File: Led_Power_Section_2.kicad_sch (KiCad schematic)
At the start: 11 parts, among them IC2 A6214KLKTR-T

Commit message: fixing review suggestions
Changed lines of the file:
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@@
 		)
 	)
-	(global_label "LED_6"
-		(shape input)
+	(hierarchical_label "LED_6"
+		(shape output)
 		(at 118.11 40.64 0)
 		(fields_autoplaced yes)
@@
 			(justify left)
 		)
-		(property "Intersheetrefs" "${INTERSHEET_REFS}"
-			(at 126.7194 40.64 0)
-			(effects
-				(font
-					(size 1.27 1.27)
-				)
-				(justify left)
-				(hide yes)
+	)
+	(hierarchical_label "I_LED_6"
+		(shape output)
+		(at 118.11 33.02 0)
+		(fields_autoplaced yes)
+		(effects
+			(font
+				(size 1.27 1.27)
 			)
+			(justify left)
 		)
 	)
-	(global_label "ADIM_0"
+	(hierarchical_label "ADIM_0"
 		(shape input)
 		(at 53.34 39.37 180)
@@
 			(justify right)
 		)
-		(property "Intersheetrefs" "${INTERSHEET_REFS}"
-			(at 43.7629 39.37 0)
-			(effects
-				(font
-					(size 1.27 1.27)
-				)
-				(justify right)
-				(hide yes)
-			)
-		)
 	)
-	(global_label "I_LED_6"
-		(shape input)
-		(at 118.11 33.02 0)
-		(fields_autoplaced yes)
-		(effects
-			(font
-				(size 1.27 1.27)
-			)
-			(justify left)
-		)
-		(property "Intersheetrefs" "${INTERSHEET_REFS}"
-			(at 128.2918 33.02 0)
-			(effects
-				(font
-					(size 1.27 1.27)
-				)
-				(justify left)
-				(hide yes)
-			)
-		)
-	)

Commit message: first complete version schematics
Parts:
- added C40, C44, C48, C52, C56: 33 uF, Capacitor_THT:CP_Radial_D8.0mm_P3.50mm, symbol PCM_SL_Devices:Capacitor_PO
- added C41, C45, C49, C53, C57: 4.7 uF, Capacitor_THT:C_Disc_D3.0mm_W2.0mm_P2.50mm, symbol PCM_SL_Devices:Capacitor_NP
- added C42, C46, C50, C54, C58: 1 uF, Capacitor_SMD:C_1206_3216Metric_Pad1.33x1.80mm_HandSolder, symbol PCM_SL_Devices:Capacitor_NP
- added C43, C47, C51, C55, C59: 0.1 uF, Capacitor_SMD:C_1206_3216Metric_Pad1.33x1.80mm_HandSolder, symbol PCM_SL_Devices:Capacitor_NP
- added D10, D11, D12, D8, D9: 30V 2A, ADC:SODFL3516X90N, symbol PCM_4ms_Diode:B140-E3
- added IC10, IC11, IC12, IC13, IC9: A6214KLKTR-T, LED_Driver:SOP100P600X165-11N, symbol A6214KLKTR-T:A6214KLKTR-T
- added L10, L11, L12, L8, L9: 47 uH 2A, ADC:CDRH105RNP151NC, symbol Device:L
- added R21, R22, R25, R26, R29, R30, R33, R34, R37, R38: 10k, Resistor_SMD:R_1206_3216Metric_Pad1.30x1.75mm_HandSolder, symbol PCM_SL_Resistors:Resistor
- added R23, R27, R31, R35, R39: 442k, Resistor_SMD:R_1206_3216Metric_Pad1.30x1.75mm_HandSolder, symbol PCM_SL_Resistors:Resistor
- added R24, R28, R32, R36, R40: R120 or R260, Resistor_THT:R_Radial_Power_L16.1mm_W9.0mm_P7.37mm, symbol PCM_SL_Resistors:Resistor
- D1: value 60V 2A -> 30V 2A
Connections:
- net +12V: now also C40.1, C41.2, C44.1, C45.2, C48.1, C49.2, C52.1, C53.2, C56.1, C57.2, IC10.1 (VIN), IC11.1 (VIN), IC12.1 (VIN), IC13.1 (VIN), IC9.1 (VIN), R23.2, R27.2, R31.2, R35.2, R39.2
- net +5V: now also R21.1, R25.1, R29.1, R33.1, R37.1
- net GND: now also C40.2, C41.1, C42.1, C44.2, C45.1, C46.1, C48.2, C49.1, C50.1, C52.2, C53.1, C54.1, C56.2, C57.1, C58.1, D10.2 (A), D11.2 (A), D12.2 (A), D8.2 (A), D9.2 (A), IC10.11 (GND_2), IC10.6 (GND_1), IC11.11 (GND_2), IC11.6 (GND_1), IC12.11 (GND_2), IC12.6 (GND_1), IC13.11 (GND_2), IC13.6 (GND_1), IC9.11 (GND_2), IC9.6 (GND_1), R22.2, R26.2, R30.2, R34.2, R38.2
- new net: C51.2, D10.1 (K), IC11.10 (SW), L10.1
- new net: IC9.2 (TON), R23.1
- new net: C47.2, D9.1 (K), IC10.10 (SW), L9.1
- new net: C55.1, IC12.9 (BOOT)
- new net: C55.2, D11.1 (K), IC12.10 (SW), L11.1
- new net: IC10.3 (EN/PWM), R25.2, R26.1
- new net: IC12.3 (EN/PWM), R33.2, R34.1
- new net: IC11.3 (EN/PWM), R29.2, R30.1
- new net: C59.1, IC13.9 (BOOT)
- new net: C59.2, D12.1 (K), IC13.10 (SW), L12.1
- new net: IC11.2 (TON), R31.1
- new net: IC13.2 (TON), R39.1
- new net: IC13.3 (EN/PWM), R37.2, R38.1
- new net: C58.2, IC13.5 (VCC)
- new net: C54.2, IC12.5 (VCC)
- new net: C42.2, IC9.5 (VCC)
- new net: C51.1, IC11.9 (BOOT)
- new net: IC9.3 (EN/PWM), R21.2, R22.1
- new net: C43.2, D8.1 (K), IC9.10 (SW), L8.1
- new net: C43.1, IC9.9 (BOOT)
- new net: IC12.2 (TON), R35.1
- new net: C46.2, IC10.5 (VCC)
- new net: C47.1, IC10.9 (BOOT)
- new net: IC10.2 (TON), R27.1
- new net: C50.2, IC11.5 (VCC)
- new net ADIM_1: IC9.4 (ADIM)
- new net ADIM_2: IC10.4 (ADIM)
- new net ADIM_3: IC11.4 (ADIM)
- new net ADIM_4: IC12.4 (ADIM)
- new net ADIM_5: IC13.4 (ADIM)
- new net I_LED_10: IC12.8 (CSH), L11.2, R36.2
- new net I_LED_11: IC13.8 (CSH), L12.2, R40.2
- new net I_LED_7: IC9.8 (CSH), L8.2, R24.2
- new net I_LED_8: IC10.8 (CSH), L9.2, R28.2
- new net I_LED_9: IC11.8 (CSH), L10.2, R32.2
- new net LED_10: IC12.7 (CSL), R36.1
- new net LED_11: IC13.7 (CSL), R40.1
- new net LED_7: IC9.7 (CSL), R24.1
- new net LED_8: IC10.7 (CSL), R28.1
- new net LED_9: IC11.7 (CSL), R32.1

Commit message: Changed footprints of passive elements, reviewed
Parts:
- removed C2, C40, C44, C48, C52, C56: 33 uF, Capacitor_THT:CP_Radial_D8.0mm_P3.50mm, symbol PCM_SL_Devices:Capacitor_PO
- removed C3, C41, C45, C49, C53, C57: 4.7 uF, Capacitor_THT:C_Disc_D3.0mm_W2.0mm_P2.50mm, symbol PCM_SL_Devices:Capacitor_NP
- removed C4, C42, C46, C50, C54, C58: 1 uF, Capacitor_SMD:C_1206_3216Metric_Pad1.33x1.80mm_HandSolder, symbol PCM_SL_Devices:Capacitor_NP
- removed C43, C47, C5, C51, C55, C59: 0.1 uF, Capacitor_SMD:C_1206_3216Metric_Pad1.33x1.80mm_HandSolder, symbol PCM_SL_Devices:Capacitor_NP
- added C44, C45, C46, C59, C60, C61: 22uF, Capacitor_SMD:C_0805_2012Metric_Pad1.18x1.45mm_HandSolder, symbol Device:C_Small
- added C47, C48, C49, C62, C63, C64: 4,7uF, Capacitor_SMD:C_0603_1608Metric_Pad1.08x0.95mm_HandSolder, symbol Device:C_Small
- added C50, C51, C52, C65, C66, C67: 1uF, Capacitor_SMD:C_0603_1608Metric_Pad1.08x0.95mm_HandSolder, symbol Device:C_Small
- added C53, C54, C55, C56, C57, C58, C68, C69, C70, C71, C72, C73: 100nF, Capacitor_SMD:C_0603_1608Metric_Pad1.08x0.95mm_HandSolder, symbol Device:C_Small
- D10: renamed from D8; value 30V 2A -> SS34; footprint ADC:SODFL3516X90N -> Diode_SMD:D_SMA; Specifications SCHOTTKY Diode SMA Vrrm>=40V If>=1.0A, Ifsm>=1.5A -> 40V, 2A
- D11: renamed from D10; value 30V 2A -> SS34; footprint ADC:SODFL3516X90N -> Diode_SMD:D_SMA; Specifications SCHOTTKY Diode SMA Vrrm>=40V If>=1.0A, Ifsm>=1.5A -> 40V, 2A
- D12, D9: value 30V 2A -> SS34; footprint ADC:SODFL3516X90N -> Diode_SMD:D_SMA; Specifications SCHOTTKY Diode SMA Vrrm>=40V If>=1.0A, Ifsm>=1.5A -> 40V, 2A
- D7: renamed from D1; value 30V 2A -> SS34; footprint ADC:SODFL3516X90N -> Diode_SMD:D_SMA; Specifications SCHOTTKY Diode SMA Vrrm>=40V If>=1.0A, Ifsm>=1.5A -> 40V, 2A
- D8: renamed from D11; value 30V 2A -> SS34; footprint ADC:SODFL3516X90N -> Diode_SMD:D_SMA; Specifications SCHOTTKY Diode SMA Vrrm>=40V If>=1.0A, Ifsm>=1.5A -> 40V, 2A
- R17: renamed from R2; footprint Resistor_SMD:R_1206_3216Metric_Pad1.30x1.75mm_HandSolder -> Resistor_SMD:R_0603_1608Metric_Pad0.98x0.95mm_HandSolder
- R18: renamed from R3; footprint Resistor_SMD:R_1206_3216Metric_Pad1.30x1.75mm_HandSolder -> Resistor_SMD:R_0603_1608Metric_Pad0.98x0.95mm_HandSolder
- R19: renamed from R33; footprint Resistor_SMD:R_1206_3216Metric_Pad1.30x1.75mm_HandSolder -> Resistor_SMD:R_0603_1608Metric_Pad0.98x0.95mm_HandSolder
- R20: renamed from R34; footprint Resistor_SMD:R_1206_3216Metric_Pad1.30x1.75mm_HandSolder -> Resistor_SMD:R_0603_1608Metric_Pad0.98x0.95mm_HandSolder
- R21: renamed from R25; footprint Resistor_SMD:R_1206_3216Metric_Pad1.30x1.75mm_HandSolder -> Resistor_SMD:R_0603_1608Metric_Pad0.98x0.95mm_HandSolder
- R22: renamed from R26; footprint Resistor_SMD:R_1206_3216Metric_Pad1.30x1.75mm_HandSolder -> Resistor_SMD:R_0603_1608Metric_Pad0.98x0.95mm_HandSolder
- R23: renamed from R6; footprint Resistor_SMD:R_1206_3216Metric_Pad1.30x1.75mm_HandSolder -> Resistor_SMD:R_0603_1608Metric_Pad0.98x0.95mm_HandSolder
- R24: renamed from R35; footprint Resistor_SMD:R_1206_3216Metric_Pad1.30x1.75mm_HandSolder -> Resistor_SMD:R_0603_1608Metric_Pad0.98x0.95mm_HandSolder
- R25: renamed from R27; footprint Resistor_SMD:R_1206_3216Metric_Pad1.30x1.75mm_HandSolder -> Resistor_SMD:R_0603_1608Metric_Pad0.98x0.95mm_HandSolder
- R29: renamed from R21; footprint Resistor_SMD:R_1206_3216Metric_Pad1.30x1.75mm_HandSolder -> Resistor_SMD:R_0603_1608Metric_Pad0.98x0.95mm_HandSolder
- R30: renamed from R22; footprint Resistor_SMD:R_1206_3216Metric_Pad1.30x1.75mm_HandSolder -> Resistor_SMD:R_0603_1608Metric_Pad0.98x0.95mm_HandSolder
- R31: renamed from R29; footprint Resistor_SMD:R_1206_3216Metric_Pad1.30x1.75mm_HandSolder -> Resistor_SMD:R_0603_1608Metric_Pad0.98x0.95mm_HandSolder
- R32: renamed from R30; footprint Resistor_SMD:R_1206_3216Metric_Pad1.30x1.75mm_HandSolder -> Resistor_SMD:R_0603_1608Metric_Pad0.98x0.95mm_HandSolder
- R33: renamed from R37; footprint Resistor_SMD:R_1206_3216Metric_Pad1.30x1.75mm_HandSolder -> Resistor_SMD:R_0603_1608Metric_Pad0.98x0.95mm_HandSolder
- R34: renamed from R38; footprint Resistor_SMD:R_1206_3216Metric_Pad1.30x1.75mm_HandSolder -> Resistor_SMD:R_0603_1608Metric_Pad0.98x0.95mm_HandSolder
- R35: renamed from R23; footprint Resistor_SMD:R_1206_3216Metric_Pad1.30x1.75mm_HandSolder -> Resistor_SMD:R_0603_1608Metric_Pad0.98x0.95mm_HandSolder
- R36: renamed from R31; footprint Resistor_SMD:R_1206_3216Metric_Pad1.30x1.75mm_HandSolder -> Resistor_SMD:R_0603_1608Metric_Pad0.98x0.95mm_HandSolder
- R37: renamed from R39; footprint Resistor_SMD:R_1206_3216Metric_Pad1.30x1.75mm_HandSolder -> Resistor_SMD:R_0603_1608Metric_Pad0.98x0.95mm_HandSolder
- renumbered IC9 to IC11, IC11 to IC12, IC2 to IC8, IC12 to IC9, L8 to L10, L10 to L11, L1 to L7, L11 to L8, R7 to R26, R36 to R27, R24 to R38, R32 to R39
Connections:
- net +12V: now also C44.2, C45.2, C46.2, C47.1, C48.1, C49.1, C59.2, C60.2, C61.2, C62.1, C63.1, C64.1
- net GND: now also C44.1, C45.1, C46.1, C47.2, C48.2, C49.2, C50.2, C51.2, C52.2, C56.2, C57.2, C58.2, C59.1, C60.1, C61.1, C62.2, C63.2, C64.2, C65.2, C66.2, C67.2, C71.2, C72.2, C73.2
- net LED_10: now also C57.1
- net LED_11: now also C73.1
- net LED_7: now also C71.1
- net LED_8: now also C58.1
- net LED_9: now also C72.1
- net at D11.1 (K), IC12.10 (SW), L11.1: now also C69.1
- net at D9.1 (K), IC10.10 (SW), L9.1: now also C55.1
- net at IC9.9 (BOOT): now also C54.2
- net at D8.1 (K), IC9.10 (SW), L8.1: now also C54.1
- net at D7.1 (K), IC8.10 (SW), L7.1: now also C53.1
- net at IC13.9 (BOOT): now also C70.2
- net at D12.1 (K), IC13.10 (SW), L12.1: now also C70.1
- net at IC13.5 (VCC): now also C67.1
- net at IC9.5 (VCC): now also C51.1
- net at IC11.5 (VCC): now also C65.1
- net at IC12.9 (BOOT): now also C69.2
- net at IC8.5 (VCC): now also C50.1
- net at IC8.9 (BOOT): now also C53.2
- net at D10.1 (K), IC11.10 (SW), L10.1: now also C68.1
- net at IC11.9 (BOOT): now also C68.2
- net at IC10.5 (VCC): now also C52.1
- net at IC10.9 (BOOT): now also C55.2
- net at IC12.5 (VCC): now also C66.1
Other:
- moved on the sheet: D8, D9, IC10, IC9, L8, L9, R19, R20, R21, R22, R24, R25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

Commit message: wip
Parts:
- removed C44, C45, C46, C59, C60, C61: 22uF, Capacitor_SMD:C_0805_2012Metric_Pad1.18x1.45mm_HandSolder, symbol Device:C_Small
- removed C47, C48, C49, C62, C63, C64: 4,7uF, Capacitor_SMD:C_0603_1608Metric_Pad1.08x0.95mm_HandSolder, symbol Device:C_Small
- removed C50, C51, C52, C65, C66, C67: 1uF, Capacitor_SMD:C_0603_1608Metric_Pad1.08x0.95mm_HandSolder, symbol Device:C_Small
- removed C53, C54, C55, C56, C57, C58, C68, C69, C70, C71, C72, C73: 100nF, Capacitor_SMD:C_0603_1608Metric_Pad1.08x0.95mm_HandSolder, symbol Device:C_Small
- removed D10, D11, D12, D7, D8, D9: SS34, Diode_SMD:D_SMA, symbol PCM_4ms_Diode:B140-E3
- removed IC10, IC11, IC12, IC13, IC8, IC9: A6214KLKTR-T, LED_Driver:SOP100P600X165-11N, symbol A6214KLKTR-T:A6214KLKTR-T
- removed L10, L11, L12, L7, L8, L9: 47 uH 2A, ADC:CDRH105RNP151NC, symbol Device:L
- removed R17, R18, R19, R20, R21, R22, R29, R30, R31, R32, R33, R34: 10k, Resistor_SMD:R_0603_1608Metric_Pad0.98x0.95mm_HandSolder, symbol PCM_SL_Resistors:Resistor
- removed R23, R24, R25, R35, R36, R37: 442k, Resistor_SMD:R_0603_1608Metric_Pad0.98x0.95mm_HandSolder, symbol PCM_SL_Resistors:Resistor
- removed R26, R27, R28, R38, R39, R40: R120 or R260, Resistor_THT:R_Radial_Power_L16.1mm_W9.0mm_P7.37mm, symbol PCM_SL_Resistors:Resistor
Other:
- added sheet LED_DRIVER_ADIM_1 (Led_driver_adim.kicad_sch)
- added sheet LED_DRIVER_ADIM_2 (Led_driver_adim.kicad_sch)
- added sheet LED_DRIVER_ADIM_3 (Led_driver_adim.kicad_sch)
- added sheet LED_DRIVER_ADIM_4 (Led_driver_adim.kicad_sch)
- added sheet LED_DRIVER_ADIM_5 (Led_driver_adim.kicad_sch)
- added sheet LED_DRIVER_ADIM_6 (Led_driver_adim.kicad_sch)

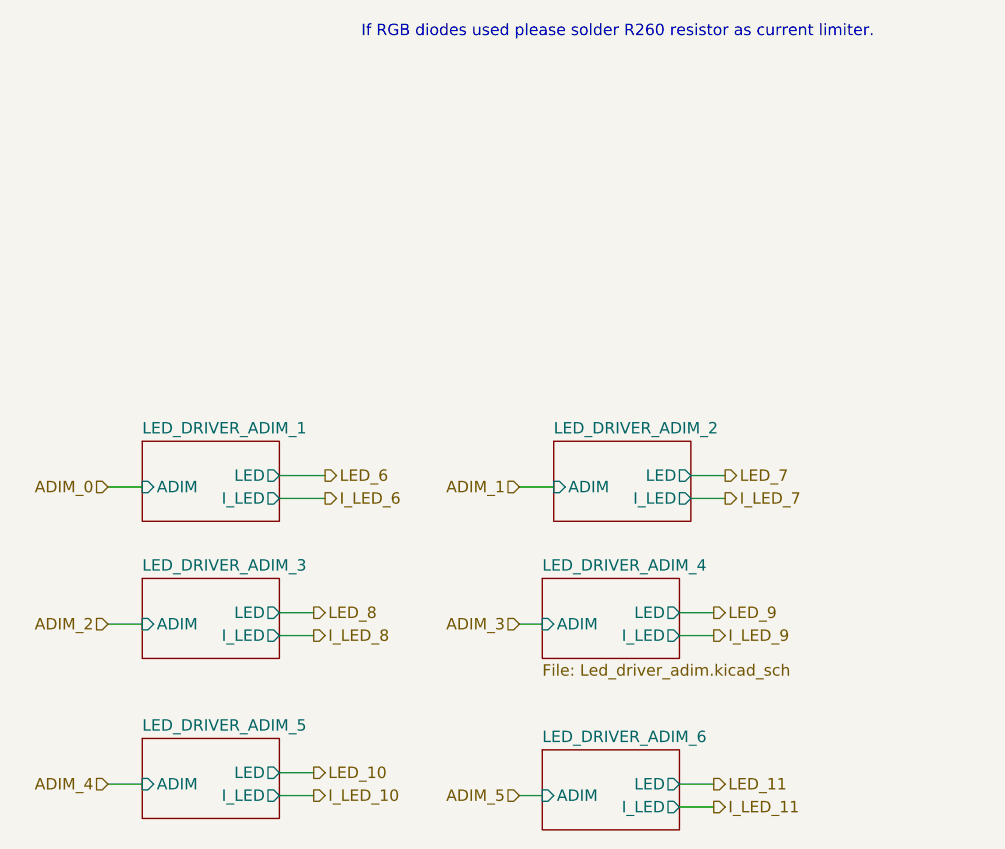
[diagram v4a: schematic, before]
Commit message: Added current sense amplifier, reduced one ADC, changed elec cap to tantals, to review
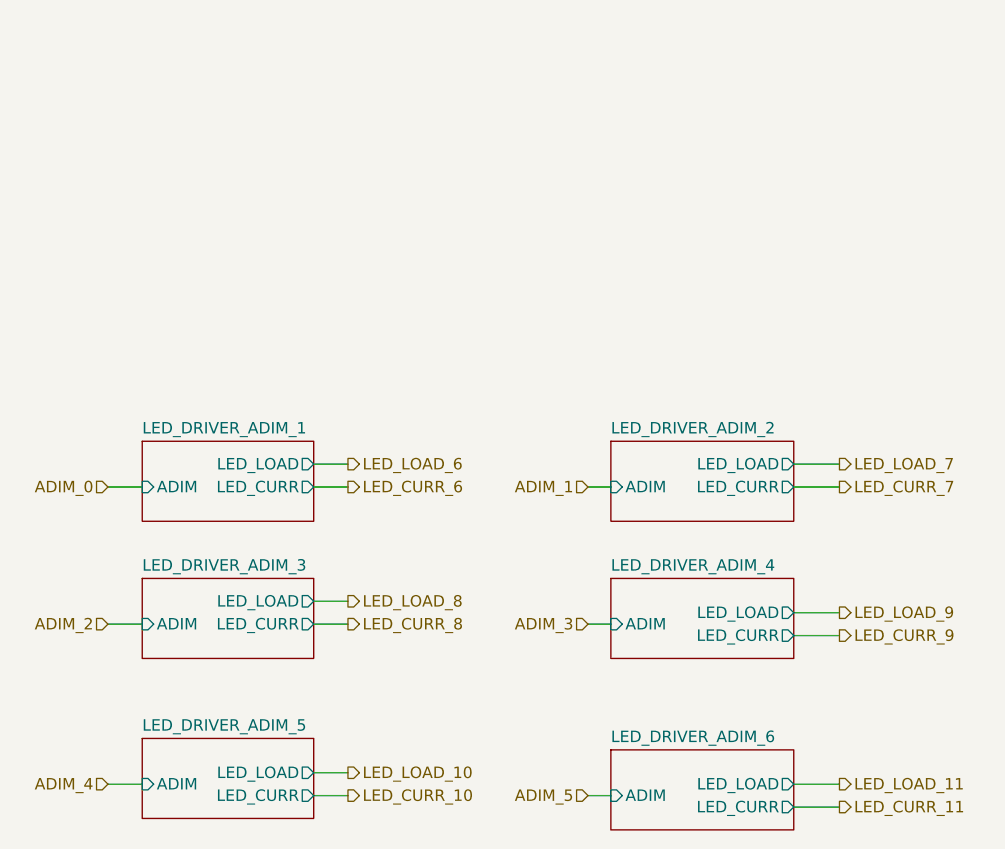
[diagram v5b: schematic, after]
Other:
- sheet LED_DRIVER_ADIM_1 ports: added LED_CURR, LED_LOAD; removed I_LED, LED
- sheet LED_DRIVER_ADIM_2 ports: added LED_CURR, LED_LOAD; removed I_LED, LED
- sheet LED_DRIVER_ADIM_3 ports: added LED_CURR, LED_LOAD; removed I_LED, LED
- sheet LED_DRIVER_ADIM_4 ports: added LED_CURR, LED_LOAD; removed I_LED, LED
- sheet LED_DRIVER_ADIM_5 ports: added LED_CURR, LED_LOAD; removed I_LED, LED
- sheet LED_DRIVER_ADIM_6 ports: added LED_CURR, LED_LOAD; removed I_LED, LED
- note removed: "If RGB diodes used please solder R260 resistor as current limiter."
